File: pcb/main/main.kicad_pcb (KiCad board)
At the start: 2 copper layers, 175.3 x 107.3 mm, 74 parts, among them J1 RJ45, J10 SWD, J2 USB_B, J3 BOOT1, J5 ROW0, J6 ROW1, J7 ROW2, J8 ROW3, J9 BOOT0, Q1 Q_PMOS_GDS, SW1 RST, SW10 K41, SW15 K42, SW20 K43, SW5 K40, U1 STM32F103C8T6, U2 ADNS-9800, U3 LM1084-3.3, Y1 32.768kHz, Y2 8M

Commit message: revise main pcb
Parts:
- removed C1, C4, C5, C6: 10uF, Capacitor_SMD:C_1206_3216Metric
- removed C10, C9: 20pF, Capacitor_SMD:C_0603_1608Metric
- removed C11: 1uF, Capacitor_SMD:C_1206_3216Metric
- removed C12, C13, C14, C15, C16: 0.1uF, Capacitor_SMD:C_0603_1608Metric
- removed C2: 470pF, Capacitor_SMD:C_1206_3216Metric
- removed C7, C8: 12.5pF, Capacitor_SMD:C_0603_1608Metric
- removed D1, D2, D3: LED, LED_SMD:LED_0603_1608Metric
- removed D11, D16, D21, D28: D, Diode_SMD:D_SOD-123
- removed J1: RJ45, folivora:RJ45_rev
- removed J10: SWD, Connector_PinHeader_2.54mm:PinHeader_1x04_P2.54mm_Horizontal
- removed J9: BOOT0, Connector_PinHeader_2.54mm:PinHeader_1x03_P2.54mm_Vertical
- removed JP2, JP3, JP4: L, Jumper:SolderJumper-2_P1.3mm_Open_Pad1.0x1.5mm
- removed JP5, JP6, JP7, JP8: R, Jumper:SolderJumper-2_P1.3mm_Open_Pad1.0x1.5mm
- removed Q1: Q_PMOS_GDS, Package_TO_SOT_SMD:SOT-223-3_TabPin2
- removed R1: 10Mohm, Resistor_SMD:R_0603_1608Metric
- removed R2: 4.7kohm, Resistor_SMD:R_0603_1608Metric
- removed R3, R4: 10kohm, Resistor_SMD:R_0603_1608Metric
- removed R5: 1.5kohm, Resistor_SMD:R_0603_1608Metric
- removed R6, R7, R8: 140ohm, Resistor_SMD:R_0603_1608Metric
- removed the REF** at (151.8, 157.5)
- removed the REF** at (130.8, 136.5)
- removed the REF** at (109.9, 157.5)
- removed the REF** at (130.8, 178.4)
- removed the REF** at (151.8, 147.3)
- removed SW10: K41, folivora:SW_Cherry_MX1A_1.00u_PCB
- removed SW15: K42, folivora:SW_Cherry_MX1A_1.00u_PCB
- removed SW20: K43, folivora:SW_Cherry_MX1A_1.00u_PCB
- removed SW5: K40, folivora:SW_Cherry_MX1A_1.00u_PCB
- removed U1: STM32F103C8T6, Package_QFP:LQFP-48_7x7mm_P0.5mm
- removed U3: LM1084-3.3, Package_TO_SOT_SMD:TO-252-3_TabPin2
- removed Y1: 32.768kHz, Crystal:Crystal_DS26_D2.0mm_L6.0mm_Horizontal
- removed Y2: 8M, Crystal:Crystal_HC49-U_Vertical
- added D7: LED, LED_THT:LED_D3.0mm, F.Cu at (251.0, 99.6)
- added J4: ROW0, Connector_JST:JST_XH_S07B-XH-A_1x07_P2.50mm_Horizontal, B.Cu at (201.3, 90.2)
- added SW2: SW41, folivora:SW_Cherry_MX1A_1.00u_PCB, F.Cu at (134.6, 168.9)
- added SW3: SW42, folivora:SW_Cherry_MX1A_1.00u_PCB, F.Cu at (157.5, 165.1)
- added SW4: SW43, folivora:SW_Cherry_MX1A_1.00u_PCB, F.Cu at (179.1, 168.9)
- C3: value 10uF -> 0.1uF; footprint Capacitor_SMD:C_1206_3216Metric -> Capacitor_SMD:C_0603_1608Metric
- D5, D6: value D -> LED; footprint Diode_SMD:D_SOD-123 -> LED_THT:LED_D3.0mm
- J3: value BOOT1 -> Trackball_conn; footprint Connector_PinHeader_2.54mm:PinHeader_1x03_P2.54mm_Vertical -> Connector_JST:JST_XH_S06B-XH-A_1x06_P2.50mm_Horizontal; moved to B.Cu
- J5: value ROW0 -> RJ45; footprint Connector_JST:JST_XH_S07B-XH-A-1_1x07_P2.50mm_Horizontal -> folivora:RJ45_rev
- J6, J7, J8: footprint Connector_JST:JST_XH_S07B-XH-A-1_1x07_P2.50mm_Horizontal -> Connector_JST:JST_XH_S07B-XH-A_1x07_P2.50mm_Horizontal; moved to B.Cu
- JP1: value L -> slave; footprint Jumper:SolderJumper-2_P1.3mm_Open_Pad1.0x1.5mm -> Connector_JST:JST_XH_S02B-XH-A_1x02_P2.50mm_Horizontal; moved to B.Cu
- SW1: value RST -> SW40; footprint Button_Switch_SMD:SW_SPST_TL3305A -> folivora:SW_Cherry_MX1A_1.00u_PCB
- U2: value ADNS-9800 -> BlackPill; footprint folivora:ADNS-9800 -> folivora:BlackPill
- moved D6 152.7 mm to (255.5, 99.6), turned to 90 degrees
- moved D5 127.8 mm to (260.1, 99.6)
- moved J2 122.3 mm to (238.8, 97.5)
- moved J5 81.7 mm to (114.9, 151.8), turned to 270 degrees
- moved JP1 79.0 mm to (110.5, 170.1), turned to 90 degrees
- moved U2 74.2 mm to (106.0, 95.2), turned to 0 degrees
- moved J6 66.6 mm to (224.8, 102.2), turned to 270 degrees
- moved SW1 62.9 mm to (114.3, 179.1), turned to 30 degrees
- moved J3 55.8 mm to (154.4, 145.8), turned to 180 degrees
- moved J7 48.3 mm to (238.8, 120.0), turned to 270 degrees
- moved J8 45.9 mm to (225.0, 136.1), turned to 270 degrees
- moved C3 21.7 mm to (108.0, 134.6), turned to 270 degrees
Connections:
- C3 pad 1: GND -> +3V3
- C3 pad 2: +3V3 -> GND
- D5 pad 1: Net-(C4-Pad2) -> GND
- D5 pad 2: +3V3 -> Net-(D5-Pad2)
- D6 pad 1: Net-(D6-Pad1) -> GND
- D6 pad 2: /COL0 -> Net-(D6-Pad2)
- J2 pad 1: /USB_1 -> +5V
- J2 pad 2: /USB_2 -> /D-
- J2 pad 3: /USB_3 -> /D+
- J2 pad 4: /USB_4 -> GND
- J3 pad 2: /BOOT1 -> /SS_T
- J3 pad 3: GND -> /SCK
- J5 pad 1: /ROW0 -> GND
- J5 pad 2: /COL0 -> Net-(J5-Pad2)
- J5 pad 3: /COL1 -> /SCK
- J5 pad 4: /COL2 -> /MOSI
- J5 pad 5: /COL3 -> /MISO
- J5 pad 6: /COL4 -> /SS_K
- J5 pad 7: /COL5 -> /SS_T
- J6 pad 1: /ROW1 -> /SELECT1
- J6 pad 2: /COL0 -> /READ0
- J6 pad 3: /COL1 -> /READ1
- J6 pad 4: /COL2 -> /READ2
- J6 pad 5: /COL3 -> /READ3
- J6 pad 6: /COL4 -> /READ4
- J6 pad 7: /COL5 -> /READ5
- J7 pad 1: /ROW2 -> /SELECT2
- J7 pad 2: /COL0 -> /READ0
- J7 pad 3: /COL1 -> /READ1
- J7 pad 4: /COL2 -> /READ2
- J7 pad 5: /COL3 -> /READ3
- J7 pad 6: /COL4 -> /READ4
- J7 pad 7: /COL5 -> /READ5
- J8 pad 1: /ROW3 -> /SELECT3
- J8 pad 2: /COL0 -> /READ0
- J8 pad 3: /COL1 -> /READ1
- J8 pad 4: /COL2 -> /READ2
- J8 pad 5: /COL3 -> /READ3
- J8 pad 6: /COL4 -> /READ4
- J8 pad 7: /COL5 -> /READ5
- JP1 pad 1: +5V -> Net-(JP1-Pad1)
- JP1 pad 2: /USB_1 -> /SS_K
- SW1 pad 1: GND -> Net-(D1-Pad1)
- SW1 pad 2: Net-(C11-Pad1) -> /SELECT4
- U2 pad 1: Net-(C2-Pad1) -> /SELECT0
- U2 pad 10: +3V3 -> /READ0
- U2 pad 11: GND -> /READ1
- U2 pad 12: +3V3 -> /READ2
- U2 pad 13: Net-(U2-Pad13) -> /READ3
- U2 pad 14: GND -> /READ4
- U2 pad 15: +3V3 -> /READ5
- U2 pad 16: Net-(C2-Pad2) -> +3V3
- U2 pad 2: Net-(Q1-Pad1) -> /SELECT1
- U2 pad 3: /SS_Track -> /SELECT2
- U2 pad 4: /MISO -> /SELECT3
- U2 pad 5: /SCK -> /SELECT4
- U2 pad 6: /MOSI -> Net-(U2-Pad6)
- U2 pad 8: Net-(C2-Pad2) -> /D+
- U2 pad 9: +3V3 -> /D-
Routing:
- net +3V3: track 300.5 -> 0.00 mm, vias 10 -> 0
- net GND: track 280.7 -> 0.00 mm, vias 4 -> 0
- net /COL0: track 225.2 -> 0.00 mm, vias 4 -> 0
- net /COL1: track 203.3 -> 0.00 mm, vias 2 -> 0
- net /COL2: track 179.0 -> 0.00 mm, vias 2 -> 0
- net /COL3: track 167.5 -> 0.00 mm, vias 1 -> 0
- net /COL4: track 150.0 -> 0.00 mm, vias 1 -> 0
- net /COL5: track 148.9 -> 0.00 mm, vias 1 -> 0
- net /ROW3: track 113.6 -> 0.00 mm, vias 2 -> 0
- net /ROW4: track 112.3 -> 0.00 mm
- net /SCK: track 111.8 -> 0.00 mm, vias 8 -> 0
- net /SS_Track: track 111.8 -> 0.00 mm, vias 4 -> 0
- net /MOSI: track 103.3 -> 0.00 mm, vias 7 -> 0
- net /ROW2: track 97.1 -> 0.00 mm, vias 2 -> 0
- net /MISO: track 94.8 -> 0.00 mm, vias 7 -> 0
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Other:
- board size 175.3 x 107.3 mm -> 163.3 x 106.7 mm

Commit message: arrange parts
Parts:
- removed the REF** at (259.4, 147.3)
- removed the REF** at (259.4, 128.3)
- removed the REF** at (259.4, 109.2)
- added C1: 10uF, Capacitor_SMD:C_1206_3216Metric, F.Cu at (119.4, 127.0)
- added C2: 10uF, Capacitor_SMD:C_1206_3216Metric, F.Cu at (116.3, 124.0)
- added C4: 10uF, Capacitor_SMD:C_1206_3216Metric, F.Cu at (111.1, 135.3)
- added D1: D, Diode_SMD:D_SOD-123, F.Cu at (109.2, 171.4)
- added D2: D, Diode_SMD:D_SOD-123, F.Cu at (124.5, 171.7)
- added D3: D, Diode_SMD:D_SOD-123, F.Cu at (146.3, 164.6)
- added D4: D, Diode_SMD:D_SOD-123, F.Cu at (169.2, 162.6)
- added J1: Conn_01x04, Connector_PinSocket_2.54mm:PinSocket_1x04_P2.54mm_Vertical, F.Cu at (111.8, 106.7)
- added JP10: R, Jumper:SolderJumper-2_P1.3mm_Open_TrianglePad1.0x1.5mm, B.Cu at (111.8, 110.5)
- added JP11: L, Jumper:SolderJumper-2_P1.3mm_Open_TrianglePad1.0x1.5mm, F.Cu at (111.8, 110.5)
- added JP12: R, Jumper:SolderJumper-2_P1.3mm_Open_TrianglePad1.0x1.5mm, B.Cu at (114.3, 110.5)
- added JP13: L, Jumper:SolderJumper-2_P1.3mm_Open_TrianglePad1.0x1.5mm, F.Cu at (114.3, 110.5)
- added JP14: R, Jumper:SolderJumper-2_P1.3mm_Open_TrianglePad1.0x1.5mm, B.Cu at (116.8, 110.5)
- added JP15: L, Jumper:SolderJumper-2_P1.3mm_Open_TrianglePad1.0x1.5mm, F.Cu at (116.8, 110.5)
- added JP16: R, Jumper:SolderJumper-2_P1.3mm_Open_TrianglePad1.0x1.5mm, B.Cu at (119.4, 110.5)
- added JP17: L, Jumper:SolderJumper-2_P1.3mm_Open_TrianglePad1.0x1.5mm, F.Cu at (119.4, 110.5)
- added JP2: L, Jumper:SolderJumper-2_P1.3mm_Open_TrianglePad1.0x1.5mm, B.Cu at (125.7, 109.2)
- added JP3: R, Jumper:SolderJumper-2_P1.3mm_Open_TrianglePad1.0x1.5mm, F.Cu at (125.7, 106.7)
- added JP4: L, Jumper:SolderJumper-2_P1.3mm_Open_TrianglePad1.0x1.5mm, B.Cu at (125.7, 106.7)
- added JP5: R, Jumper:SolderJumper-2_P1.3mm_Open_TrianglePad1.0x1.5mm, F.Cu at (125.7, 109.2)
- added JP6: L, Jumper:SolderJumper-2_P1.3mm_Open_TrianglePad1.0x1.5mm, B.Cu at (125.7, 103.5)
- added JP7: R, Jumper:SolderJumper-2_P1.3mm_Open_TrianglePad1.0x1.5mm, F.Cu at (125.7, 101.0)
- added JP8: L, Jumper:SolderJumper-2_P1.3mm_Open_TrianglePad1.0x1.5mm, B.Cu at (125.7, 101.0)
- added JP9: R, Jumper:SolderJumper-2_P1.3mm_Open_TrianglePad1.0x1.5mm, F.Cu at (125.7, 103.5)
- added R1: R, Resistor_SMD:R_0603_1608Metric, F.Cu at (106.7, 109.7)
- added R2: R, Resistor_SMD:R_0603_1608Metric, F.Cu at (104.8, 109.7)
- added R3: R, Resistor_SMD:R_0603_1608Metric, F.Cu at (102.9, 109.7)
- added R6: 10k, Resistor_SMD:R_0603_1608Metric, F.Cu at (111.1, 139.7)
- added REF**: MountingHole_3.2mm_M3, MountingHole:MountingHole_3.2mm_M3, F.Cu at (105.4, 90.2)
- added REF**: MountingHole_3.2mm_M3, MountingHole:MountingHole_3.2mm_M3, F.Cu at (125.7, 147.3)
- added REF**: MountingHole_3.2mm_M3, MountingHole:MountingHole_3.2mm_M3, F.Cu at (105.4, 147.3)
- added REF**: MountingHole_3.2mm_M3, MountingHole:MountingHole_3.2mm_M3, F.Cu at (263.5, 147.3)
- added REF**: MountingHole_3.2mm_M3, MountingHole:MountingHole_3.2mm_M3, F.Cu at (263.5, 128.3)
- added REF**: MountingHole_3.2mm_M3, MountingHole:MountingHole_3.2mm_M3, F.Cu at (263.5, 109.2)
- added REF**: MountingHole_3.2mm_M3, MountingHole:MountingHole_3.2mm_M3, F.Cu at (125.7, 90.2)
- added SW7: RST, Button_Switch_THT:SW_Tactile_SPST_Angled_PTS645Vx31-2LFS, F.Cu at (104.1, 139.7)
- added U1: 3.3v regul, Package_TO_SOT_SMD:TO-252-3_TabPin2, F.Cu at (109.3, 125.0)
- JP1: footprint Connector_JST:JST_XH_S02B-XH-A_1x02_P2.50mm_Horizontal -> Jumper:SolderJumper-2_P1.3mm_Open_TrianglePad1.0x1.5mm; moved to F.Cu
- moved D5 156.6 mm to (103.5, 96.0), turned to 0 degrees
- moved U2 154.7 mm to (245.4, 162.6), turned to 270 degrees
- moved D6 152.0 mm to (103.5, 100.6), turned to 0 degrees
- moved D7 147.6 mm to (103.5, 105.2), turned to 0 degrees
- moved J2 124.5 mm to (114.3, 102.2)
- moved JP1 120.2 mm to (229.9, 156.2), turned to 0 degrees
- moved C3 102.9 mm to (206.2, 165.1), turned to 180 degrees
- moved J6 45.7 mm to (270.5, 102.9)
- moved J8 45.5 mm to (270.5, 138.4)
- moved J4 36.4 mm to (237.5, 86.4)
- moved J7 31.8 mm to (270.5, 120.7)
- moved J3 6.03 mm to (153.6, 151.8)
- moved REF** 4.14 mm to (225.4, 90.2)
- moved J5 2.54 mm to (114.9, 154.3)
- moved SW3 2.29 mm to (155.6, 166.4)
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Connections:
- D5 pad 1: GND -> /LED1
- D6 pad 1: GND -> /LED2
- D7 pad 1: GND -> /LED3
- J2 pad 1: +5V -> /USB_1
- J2 pad 2: /D- -> /USB_2
- J2 pad 3: /D+ -> /USB_3
- J2 pad 4: GND -> /USB_4
- U2 pad 21: Net-(U2-Pad21) -> /RST
- U2 pad 22: Net-(U2-Pad22) -> /LED3
- U2 pad 23: Net-(U2-Pad23) -> /LED2
- U2 pad 24: Net-(U2-Pad24) -> /LED1
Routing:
- removed copper zone on B.Cu, net GND
- removed copper zone on F.Cu, net GND
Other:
- board size 163.3 x 106.7 mm -> 172.1 x 109.2 mm

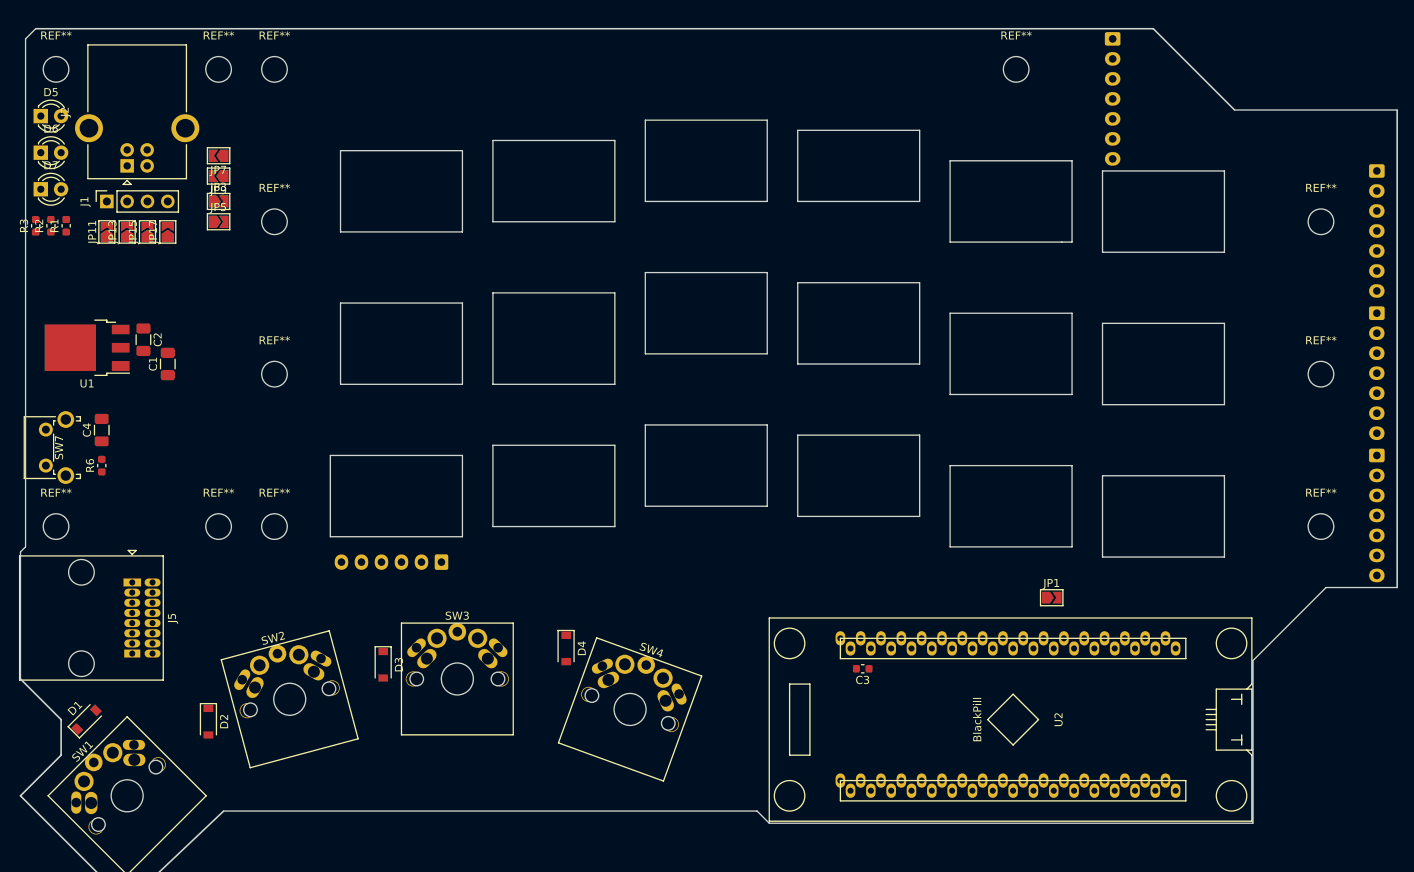
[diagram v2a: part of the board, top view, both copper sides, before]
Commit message: use STM32F103C8T6 directly
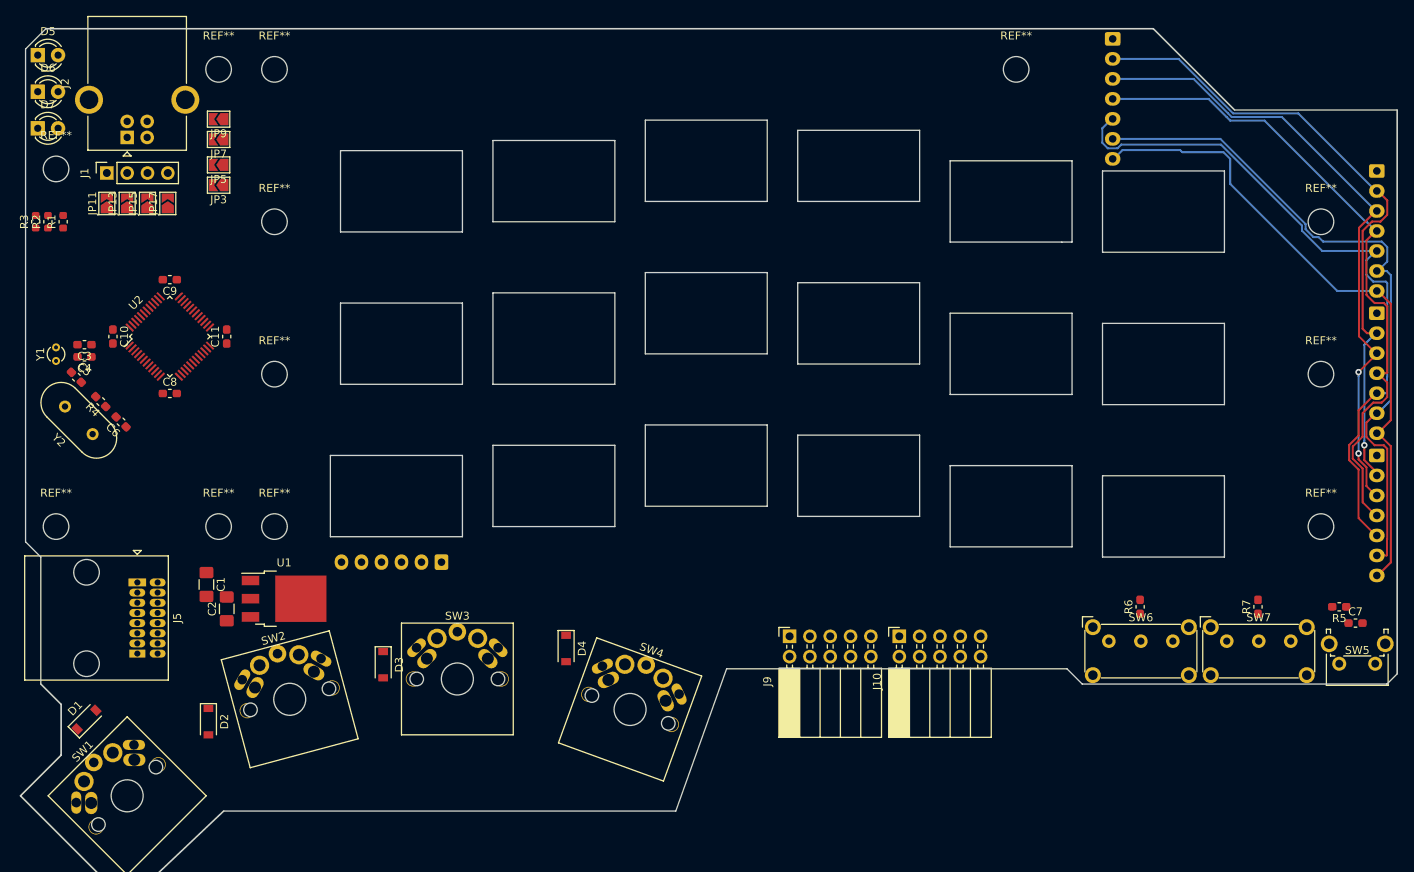
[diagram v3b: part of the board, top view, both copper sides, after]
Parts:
- removed JP1: slave, Jumper:SolderJumper-2_P1.3mm_Open_TrianglePad1.0x1.5mm
- added C10: 0.1uF, Capacitor_SMD:C_0603_1608Metric_Pad1.05x0.95mm_HandSolder, F.Cu at (112.5, 123.6)
- added C11: 0.1uF, Capacitor_SMD:C_0603_1608Metric_Pad1.05x0.95mm_HandSolder, F.Cu at (126.7, 123.6)
- added C5: 20pF, Capacitor_SMD:C_0603_1608Metric_Pad1.05x0.95mm_HandSolder, F.Cu at (108.0, 128.7)
- added C6: 20pF, Capacitor_SMD:C_0603_1608Metric_Pad1.05x0.95mm_HandSolder, F.Cu at (113.5, 134.2)
- added C7: 10uF, Capacitor_SMD:C_0603_1608Metric_Pad1.05x0.95mm_HandSolder, F.Cu at (267.8, 159.4)
- added C8: 0.1uF, Capacitor_SMD:C_0603_1608Metric_Pad1.05x0.95mm_HandSolder, F.Cu at (119.6, 130.7)
- added C9: 0.1uF, Capacitor_SMD:C_0603_1608Metric_Pad1.05x0.95mm_HandSolder, F.Cu at (119.6, 116.5)
- added J10: JTAG, Connector_PinSocket_2.54mm:PinSocket_2x05_P2.54mm_Horizontal, F.Cu at (210.8, 161.0)
- added J9: STLink, Connector_PinSocket_2.54mm:PinSocket_2x05_P2.54mm_Horizontal, F.Cu at (197.1, 161.0)
- added R4: 10Mohm, Resistor_SMD:R_0603_1608Metric_Pad1.05x0.95mm_HandSolder, F.Cu at (111.0, 131.7)
- added R5: 10kohm, Resistor_SMD:R_0603_1608Metric_Pad1.05x0.95mm_HandSolder, F.Cu at (265.8, 157.4)
- added R7: 10kohm, Resistor_SMD:R_0603_1608Metric_Pad1.05x0.95mm_HandSolder, F.Cu at (255.7, 157.4)
- added SW5: RST_SW, Button_Switch_THT:SW_Tactile_SPST_Angled_PTS645Vx31-2LFS, F.Cu at (270.3, 164.5)
- added SW6: BOOT0, Button_Switch_THT:SW_E-Switch_EG1224_SPDT_Angled, F.Cu at (237.0, 161.6)
- added Y1: 32.768kHz, Crystal:Crystal_DS15_D1.5mm_L5.0mm_Vertical, F.Cu at (105.4, 126.6)
- added Y2: 8MHz, Crystal:Crystal_HC49-U_Vertical, F.Cu at (110.0, 135.8)
- C1, C2: footprint Capacitor_SMD:C_1206_3216Metric -> Capacitor_SMD:C_1206_3216Metric_Pad1.42x1.75mm_HandSolder
- C3: value 0.1uF -> 12.5pF; footprint Capacitor_SMD:C_0603_1608Metric -> Capacitor_SMD:C_0603_1608Metric_Pad1.05x0.95mm_HandSolder
- C4: value 10uF -> 12.5pF[; footprint Capacitor_SMD:C_1206_3216Metric -> Capacitor_SMD:C_0603_1608Metric_Pad1.05x0.95mm_HandSolder
- R6: value 10k -> 10kohm; footprint Resistor_SMD:R_0603_1608Metric -> Resistor_SMD:R_0603_1608Metric_Pad1.05x0.95mm_HandSolder
- SW7: value RST -> BOOT1; footprint Button_Switch_THT:SW_Tactile_SPST_Angled_PTS645Vx31-2LFS -> Button_Switch_THT:SW_E-Switch_EG1224_SPDT_Angled
- U2: value BlackPill -> STM32F103C8Tx; footprint folivora:BlackPill -> Package_QFP:LQFP-48_7x7mm_P0.5mm
- moved SW7 149.2 mm to (251.7, 161.6), turned to 0 degrees
- moved U2 131.6 mm to (119.6, 123.6), turned to 45 degrees
- moved R6 131.0 mm to (240.9, 157.4)
- moved C3 105.4 mm to (109.0, 124.6)
- moved U1 39.9 mm to (133.9, 156.3), turned to 0 degrees
- moved C2 35.2 mm to (126.7, 157.6), turned to 90 degrees
- moved C1 28.0 mm to (124.2, 154.6), turned to 270 degrees
- moved REF** 12.4 mm to (105.4, 102.6)
- moved C4 9.40 mm to (109.0, 126.1), turned to 180 degrees
- moved D5 7.63 mm to (103.1, 88.4)
- moved D6 7.63 mm to (103.1, 93.0)
- moved D7 7.63 mm to (103.1, 97.5)
- moved JP5 7.11 mm to (125.7, 102.1), turned to 180 degrees
- moved JP9 7.11 mm to (125.7, 96.4)
- moved JP2 4.57 mm to (125.7, 104.6), turned to 180 degrees
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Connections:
- C3 pad 1: +3V3 -> GND
- C3 pad 2: GND -> /XTAL_C
- C4 pad 1: /RST -> GND
- C4 pad 2: GND -> /XTAL_D
- JP13 pad 1: /SCK -> /SCL
- JP14 pad 1: /SCK -> /SCL
- R6 pad 1: +3V3 -> Net-(R6-Pad1)
- R6 pad 2: /RST -> /BOOT0
- SW7 pad 1: /RST -> +3V3
- SW7 pad 2: GND -> Net-(R7-Pad1)
- U2 pad 1: /SELECT0 -> +3V3
- U2 pad 10: /READ0 -> /SELECT0
- U2 pad 11: /READ1 -> /SELECT1
- U2 pad 12: /READ2 -> /SELECT2
- U2 pad 13: /READ3 -> /SS_T
- U2 pad 14: /READ4 -> /SS_K
- U2 pad 15: /READ5 -> /SCK
- U2 pad 16: +3V3 -> /MISO
- U2 pad 17: GND -> /MOSI
- U2 pad 18: GND -> Net-(U2-Pad18)
- U2 pad 2: /SELECT1 -> Net-(U2-Pad2)
- U2 pad 20: Net-(U2-Pad20) -> /BOOT1
- U2 pad 21: /RST -> /LED3
- U2 pad 22: /LED3 -> /D-
- U2 pad 23: /LED2 -> GND
- U2 pad 24: /LED1 -> +3V3
- U2 pad 25: Net-(U2-Pad25) -> /D+
- U2 pad 26: Net-(JP1-Pad1) -> /READ3
- U2 pad 27: /SCK -> /READ2
- U2 pad 28: /MISO -> /READ1
- U2 pad 29: /MOSI -> /JTDI
- U2 pad 3: /SELECT2 -> /XTAL_C
- U2 pad 30: /SS_T -> /SELECT3
- U2 pad 31: /SS_K -> /SELECT4
- U2 pad 32: Net-(U2-Pad32) -> /READ5
- U2 pad 33: Net-(U2-Pad33) -> /READ4
- U2 pad 34: Net-(U2-Pad34) -> /SWDIO
- U2 pad 4: /SELECT3 -> /XTAL_D
- U2 pad 5: /SELECT4 -> /XTAL_A
- U2 pad 6: Net-(U2-Pad6) -> /XTAL_B
- U2 pad 7: Net-(U2-Pad7) -> /RST
- U2 pad 8: /D+ -> GND
- U2 pad 9: /D- -> +3V3
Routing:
- net /READ3: track 0.00 -> 86.7 mm
- net /READ4: track 0.00 -> 85.3 mm
- net /READ2: track 0.00 -> 83.4 mm
- net /READ5: track 0.00 -> 81.2 mm
- net /READ0: track 0.00 -> 80.8 mm, vias 0 -> 1
- net /READ1: track 0.00 -> 79.4 mm, vias 0 -> 2
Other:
- outline, holes or cut-outs redrawn
